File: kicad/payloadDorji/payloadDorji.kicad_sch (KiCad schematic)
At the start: 51 parts, among them J1 PWR, J2 Conn_Coaxial, J3 Conn_01x06_Male, J4 PWR, J5 UART, U1 LM386, U2 DRA818V, U3 MAX-M10M-00B, U4 NUCLEO-L432KC, U5 TPS61023DRLR, U6 AZ1117H-ADJ

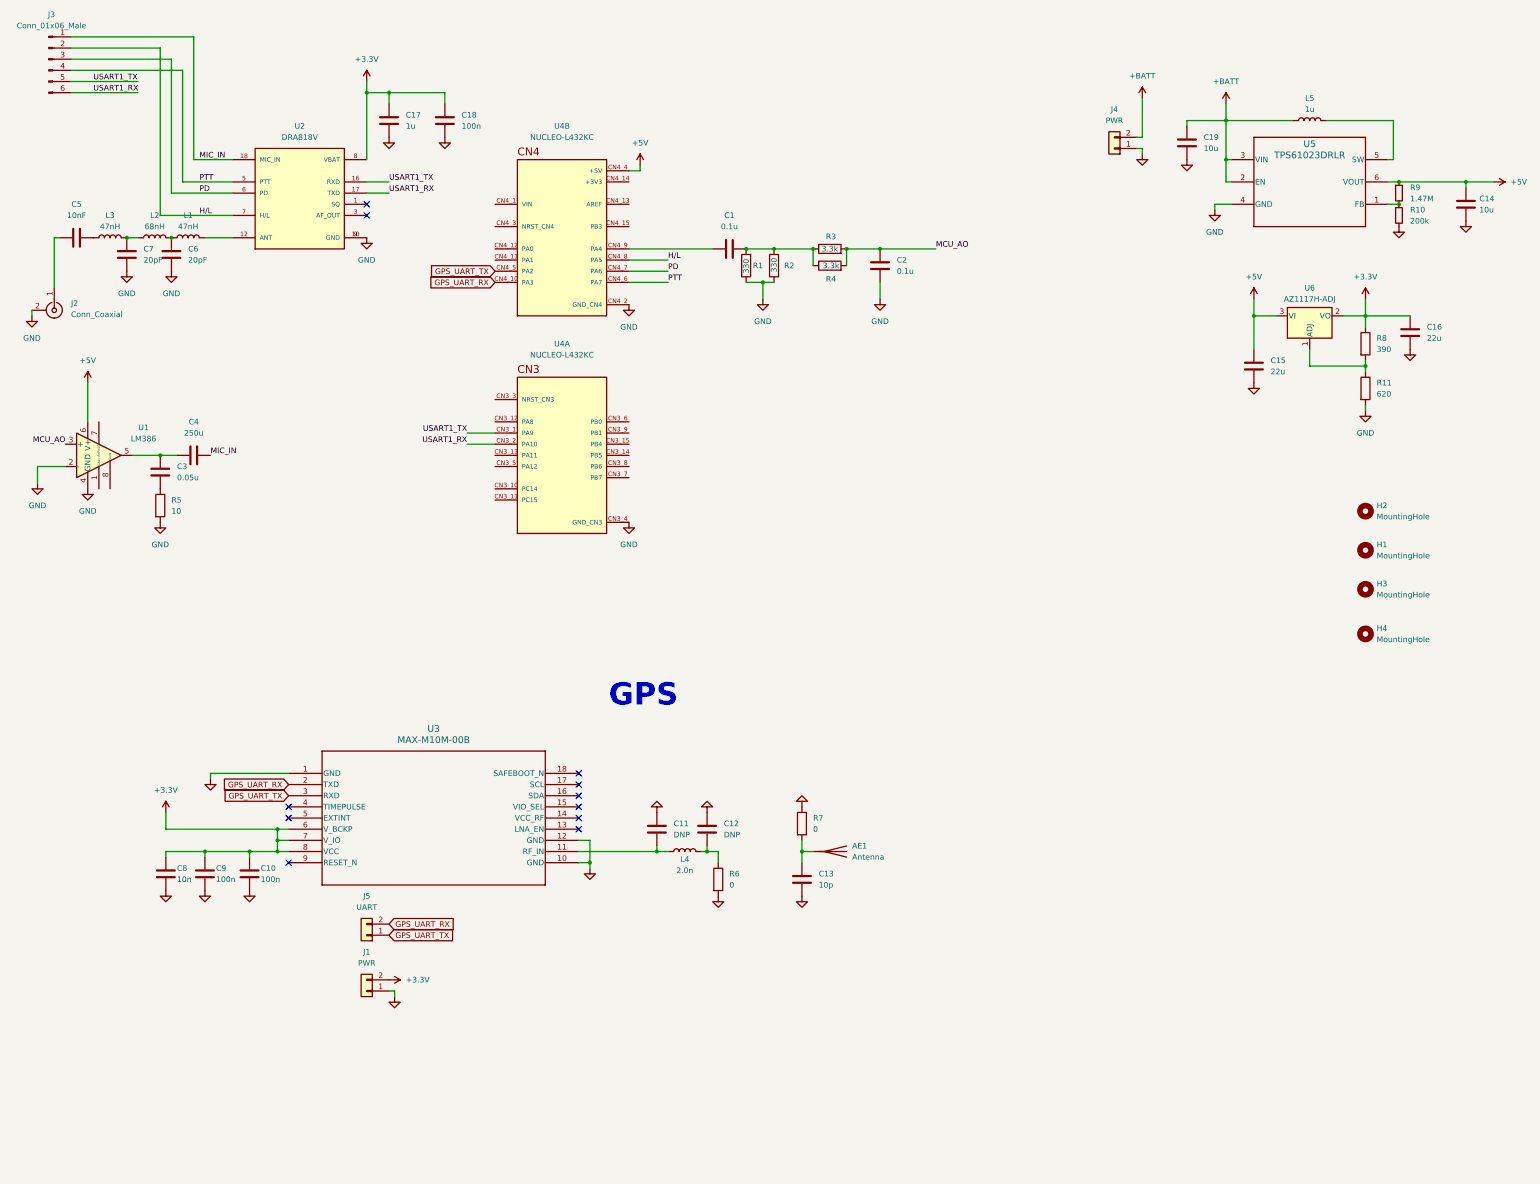
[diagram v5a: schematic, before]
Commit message: kiCAD cleanup! Added .gitignore file, removed temporary files from git, fixed library paths to be relative, cleaned up schematic errors, cleaned up layout errors, cleaned up consistency between sch/brd.
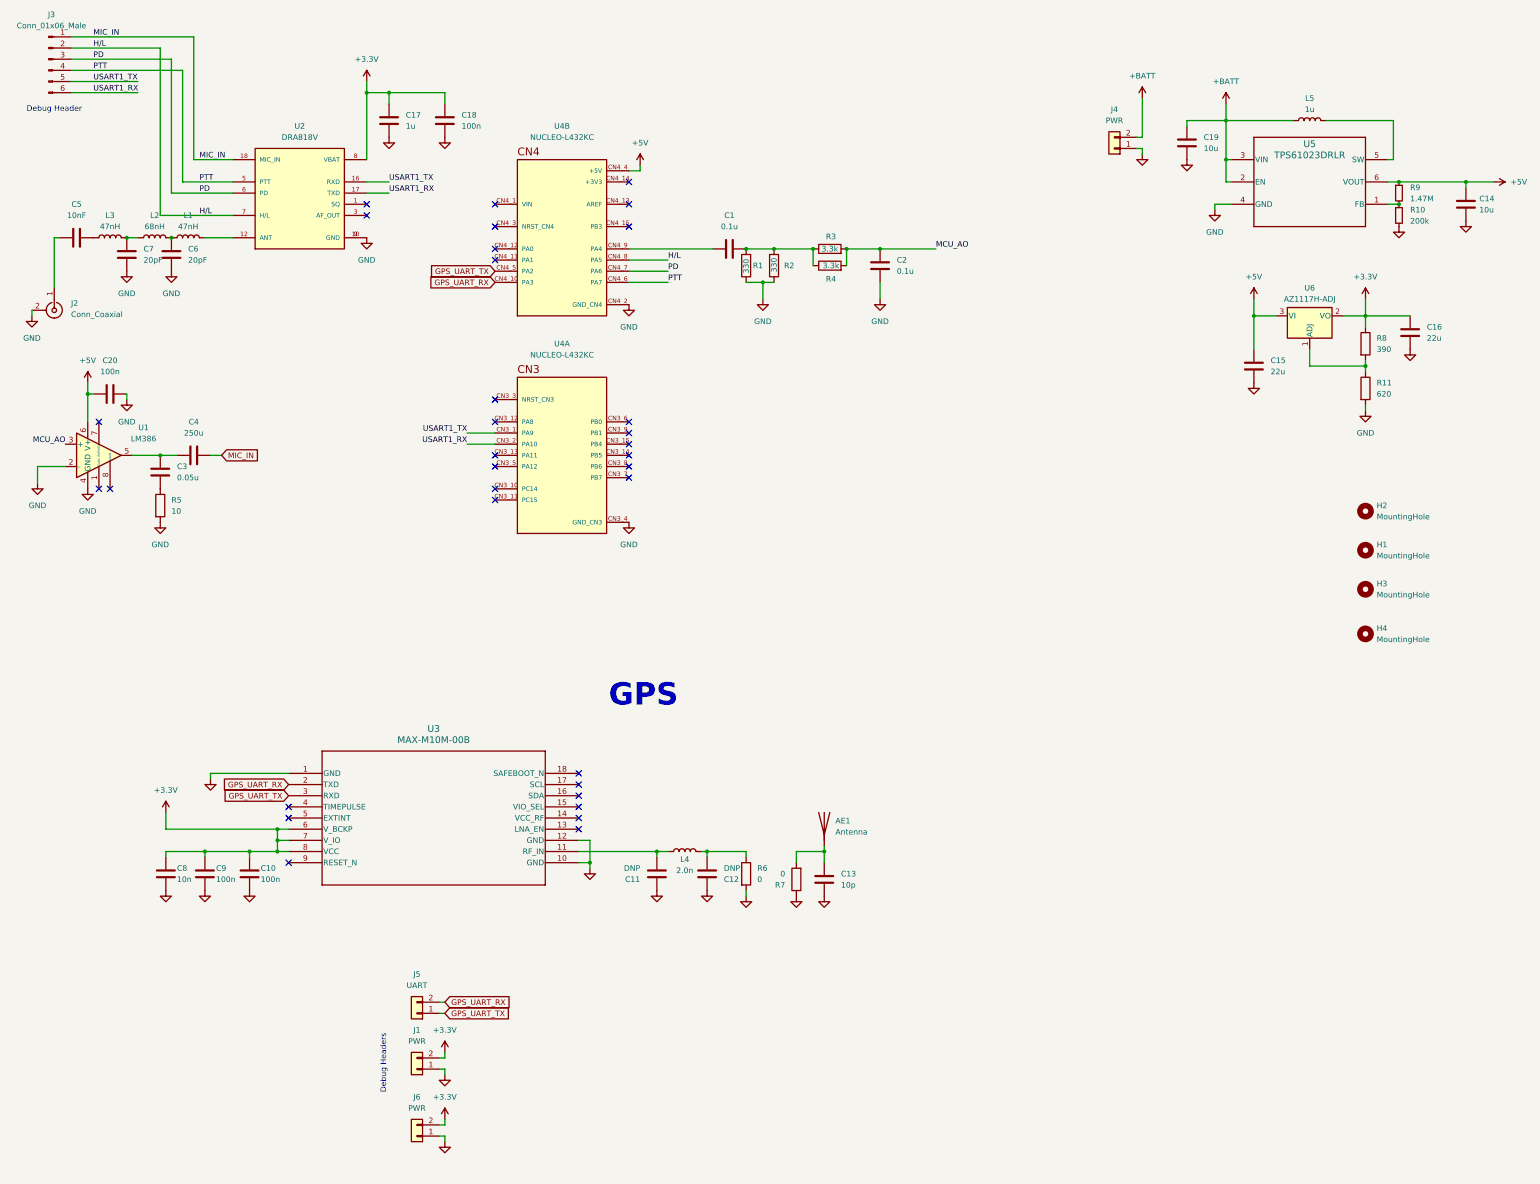
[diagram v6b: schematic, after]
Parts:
- added C20: 100n, Capacitor_SMD:C_0603_1608Metric, symbol Device:C
- added J6: PWR, Connector_PinHeader_2.54mm:PinHeader_1x02_P2.54mm_Vertical, symbol Connector_Generic:Conn_01x02
- H1, H2, H3, H4: footprint (none) -> MountingHole:MountingHole_4.3mm_M4
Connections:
- net +3.3V: now also J6.2 (Pin_2)
- net +5V: now also C20.1
- net GND: now also C20.2, J6.1 (Pin_1)
- no-connect marks 11 -> 33
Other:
- note added: "Debug Header"
- note added: "Debug Headers"
- title: (none) -> PicoAPRS
- moved on the sheet: AE1, C11, C12, C13, J1, J5, R6, R7

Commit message: Fixed library paths. Add PICOAPRS_LIBRARIES to your project variables which points to the kicad/lib directory. Also fixed up schematic to be more readable, and fixed some more issues between sch/brd.
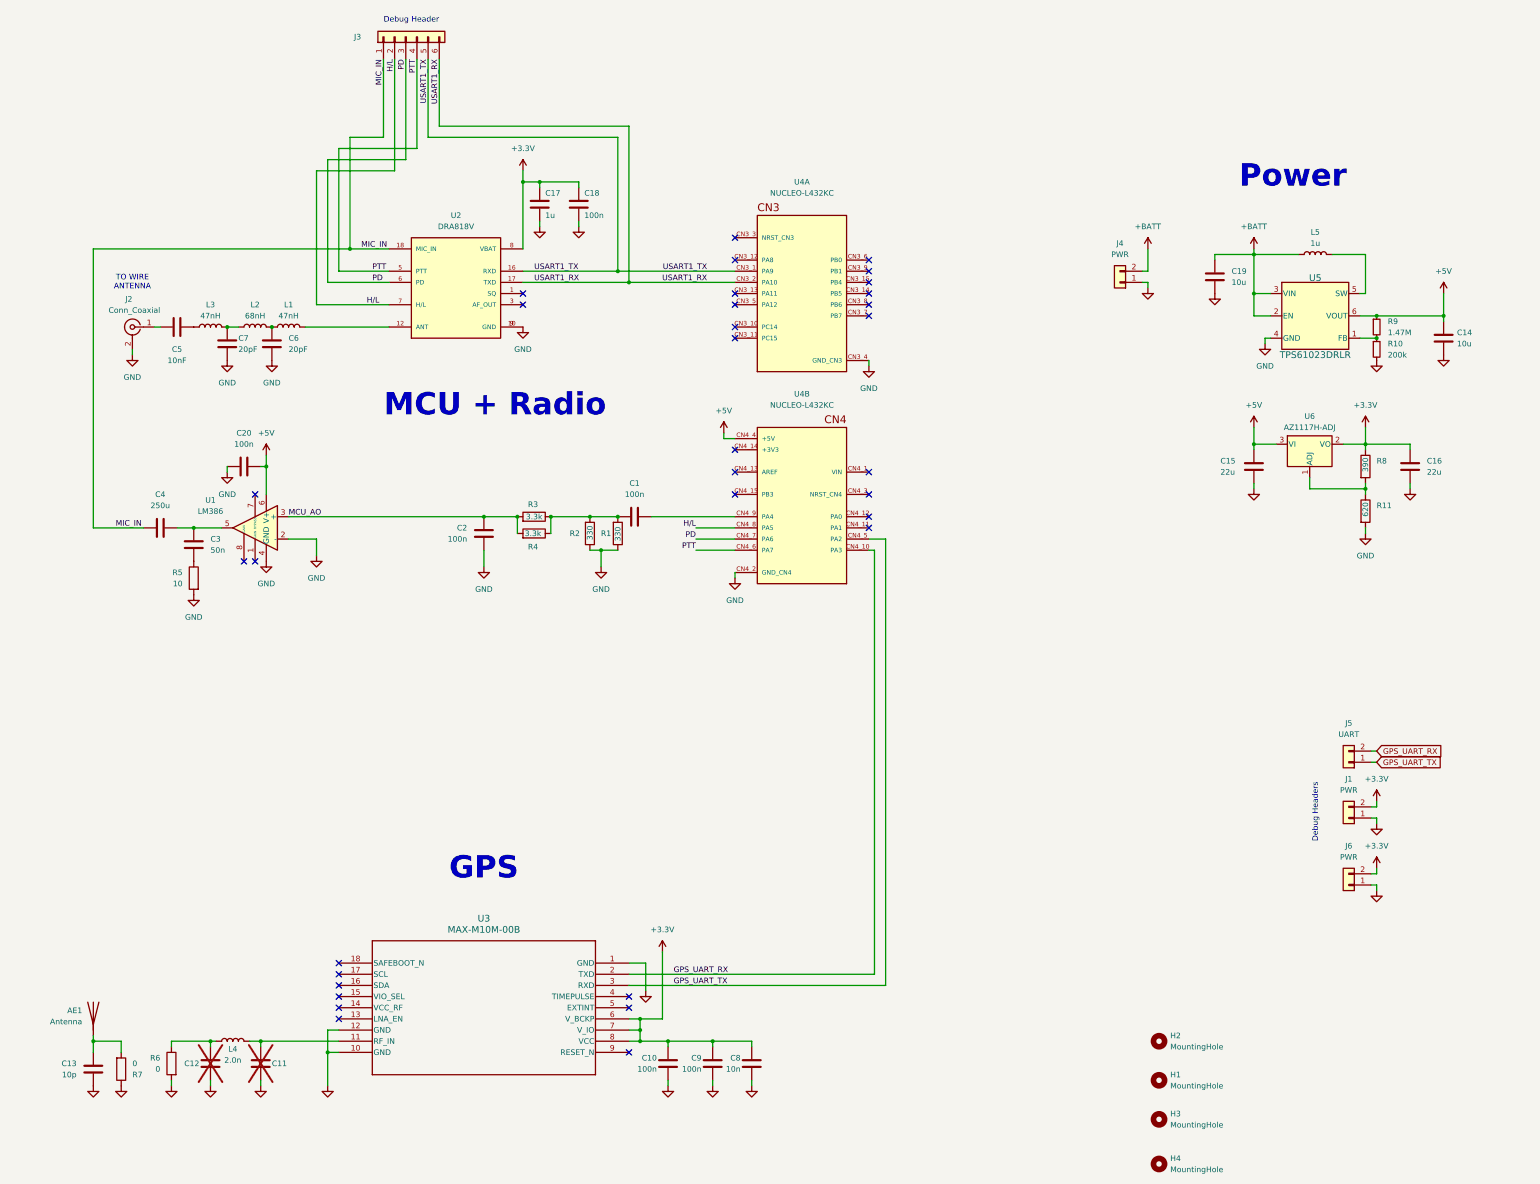
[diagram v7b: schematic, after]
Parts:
- C1, C2: value 0.1u -> 100n
- C11, C12: value DNP -> ~; now not fitted; now left out of the parts list
- C3: value 0.05u -> 50n
- J3: symbol Connector:Conn_01x06_Male -> Connector_Generic:Conn_01x06
- U5: footprint footprints:DRL0006A -> DRL0006A
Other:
- note added: "MCU + Radio"
- note added: "Power"
- note added: "TO WIRE ANTENNA"
- moved on the sheet: AE1, C1, C10, C13, C14, C15, C16, C17, C18, C19, C2, C20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

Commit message: Fixed GPS symbol (blech) and found two misconnected pins. Fixed in shcematic and layout.
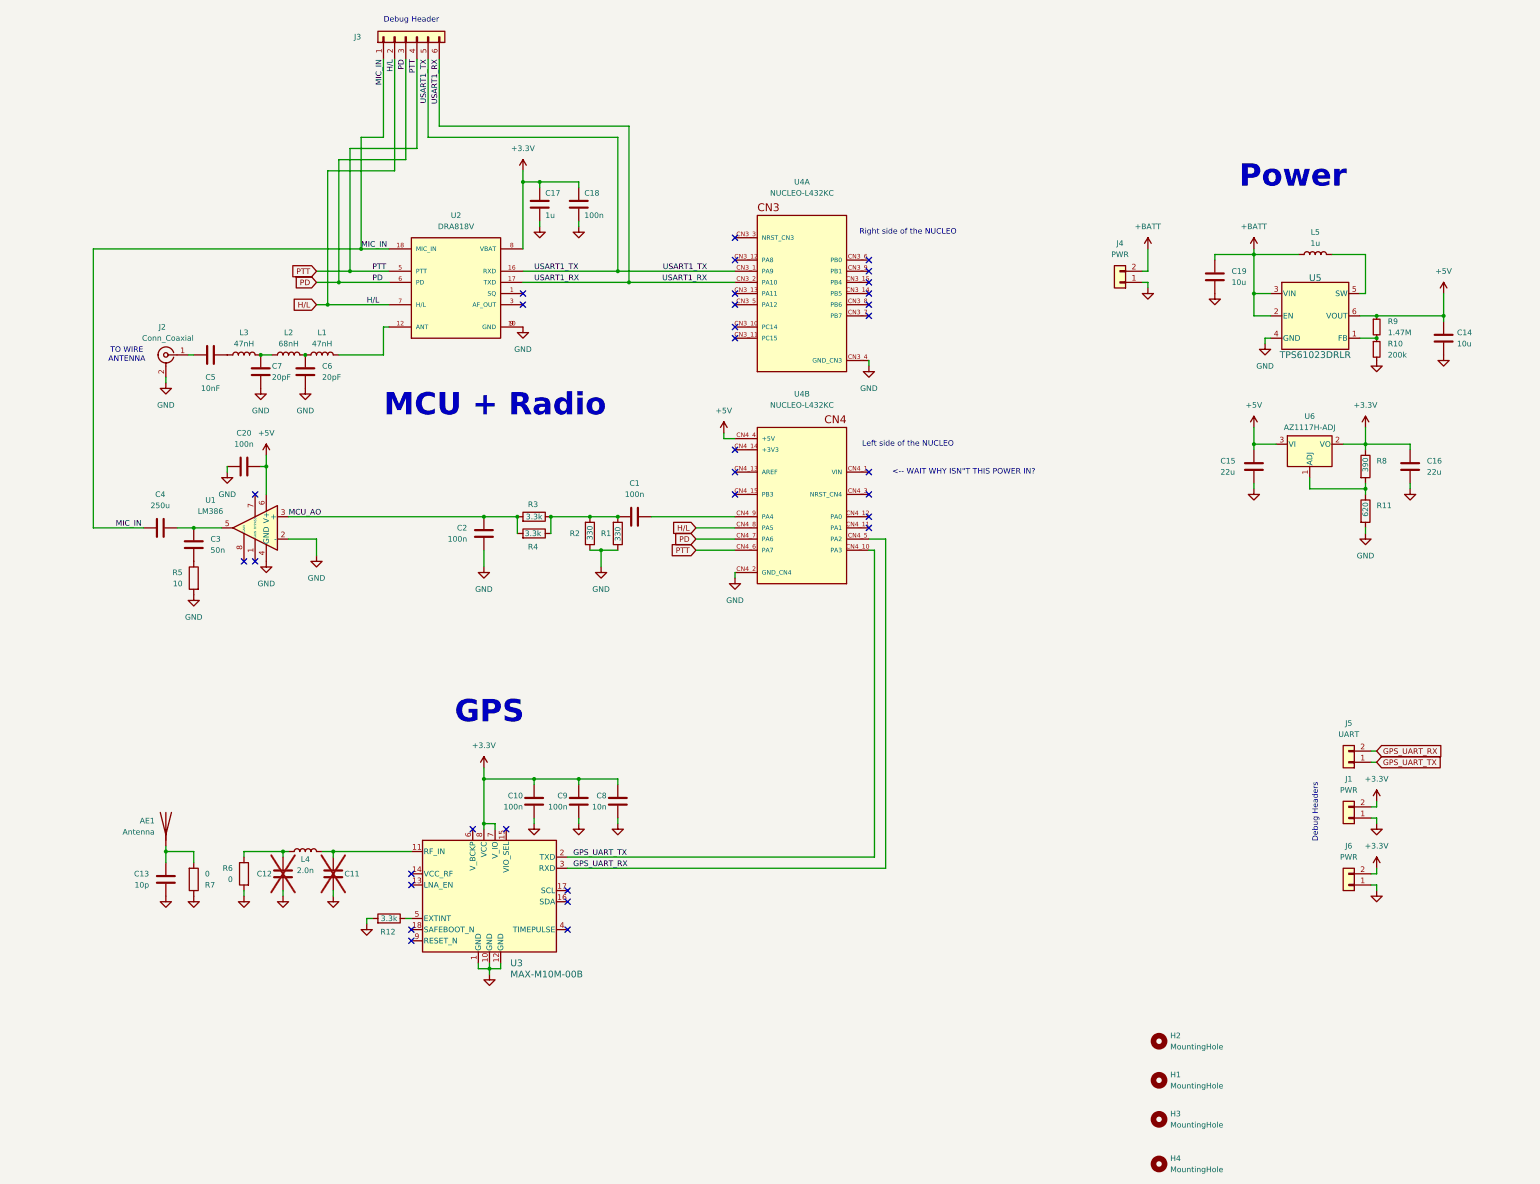
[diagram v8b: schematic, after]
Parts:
- added R12: 3.3k, Resistor_SMD:R_0603_1608Metric, symbol Device:R
- U3: footprint footprints:MOD18_MAX-M10M_UBL -> MOD18_MAX-M10M_UBL
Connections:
- net +3.3V: no longer U3.6 (V_BCKP)
- net GND: now also R12.2
- net GPS_UART_RX: now also U3.3 (RXD), U4.CN4_5 (PA2); no longer U3.2 (TXD), U4.CN4_10 (PA3)
- net GPS_UART_TX: now also U3.2 (TXD), U4.CN4_10 (PA3); no longer U3.3 (RXD), U4.CN4_5 (PA2)
- net at U3.5 (EXTINT): now also R12.1
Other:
- note added: "<-- WAIT WHY ISN"T THIS POWER IN?"
- note added: "Left side of the NUCLEO"
- note added: "Right side of the NUCLEO"
- moved on the sheet: AE1, C10, C11, C12, C13, C5, C6, C7, C8, C9, J2, L1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
